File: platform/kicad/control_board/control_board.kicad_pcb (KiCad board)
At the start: 2 copper layers, 131.5 x 81.5 mm, 55 parts, among them J1 DHT22, J10 ADC1,7, J11 Qwiic JST, J13 PJ-002A, J14 ROUTER 24V, J15 24V/5V OUT, J16 Conn_01x05_Pin, J2 DS18B20, J4 24V IN, J5 USB4120-03-C_REVA, J8 UART, J9 ADC1,6, K1 LCA717, K2 LCA717, K3 LCA717, K4 LCA717, U1 ESP32-DevKitC, U2 ACS722xLCTR-20AU, U3 AP63205WU-7

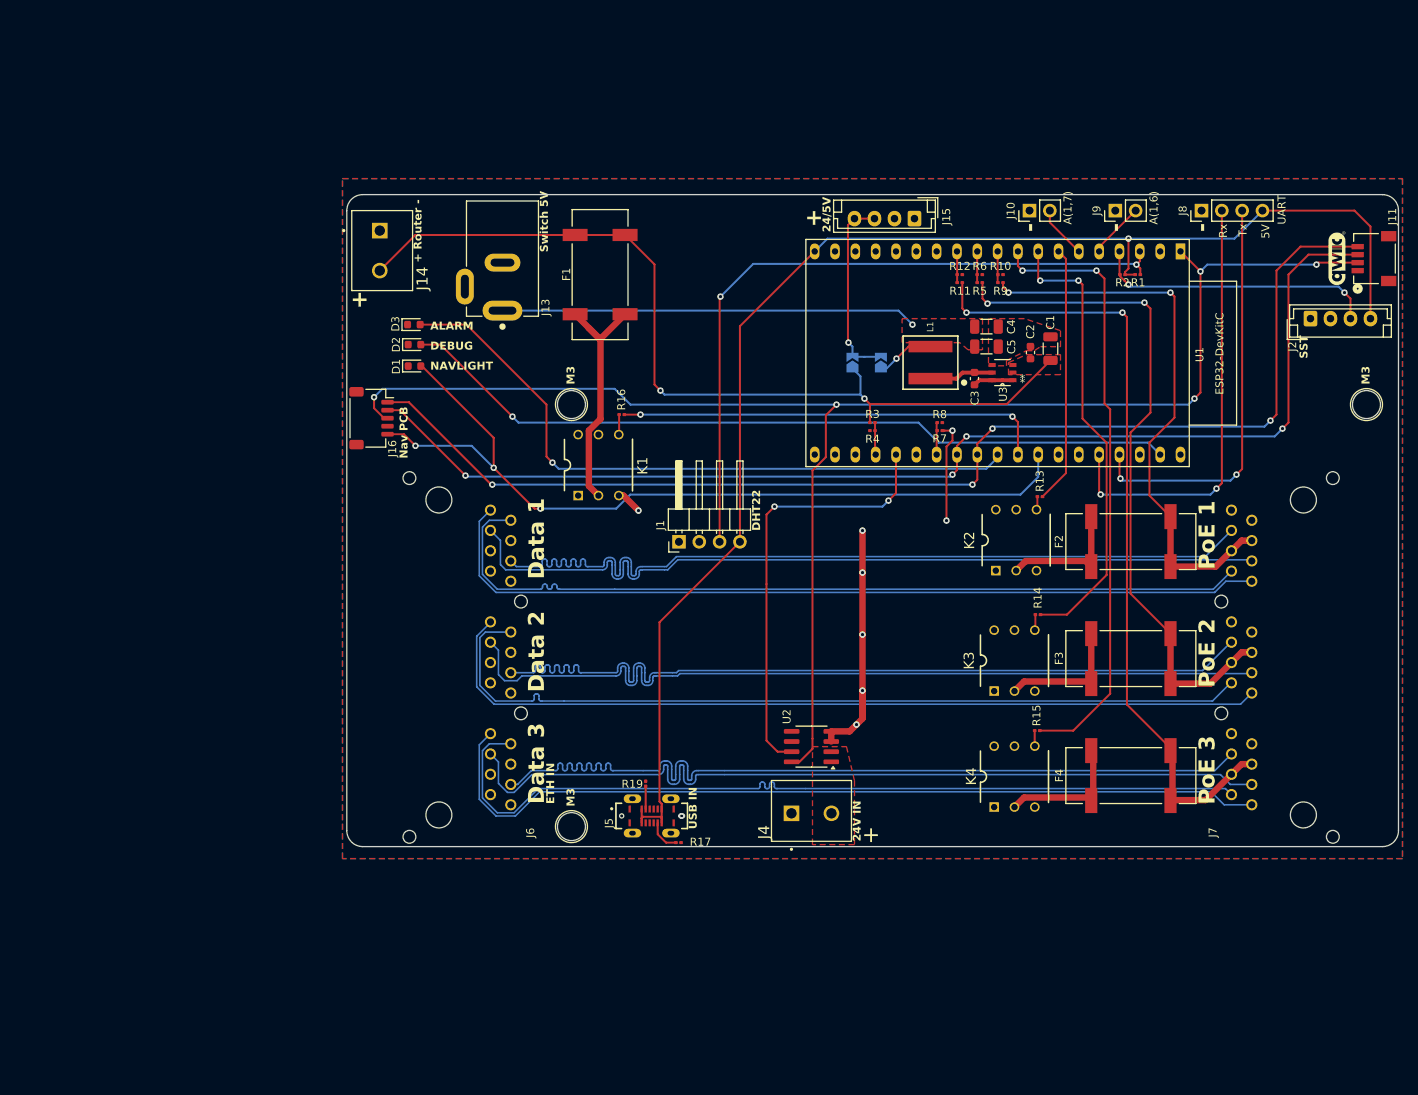
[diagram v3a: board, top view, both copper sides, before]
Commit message: Controller: Finalise Layout and Labelling (#3)
This change finalises the layout and tracks for the controller PCB, as well as the labelling.
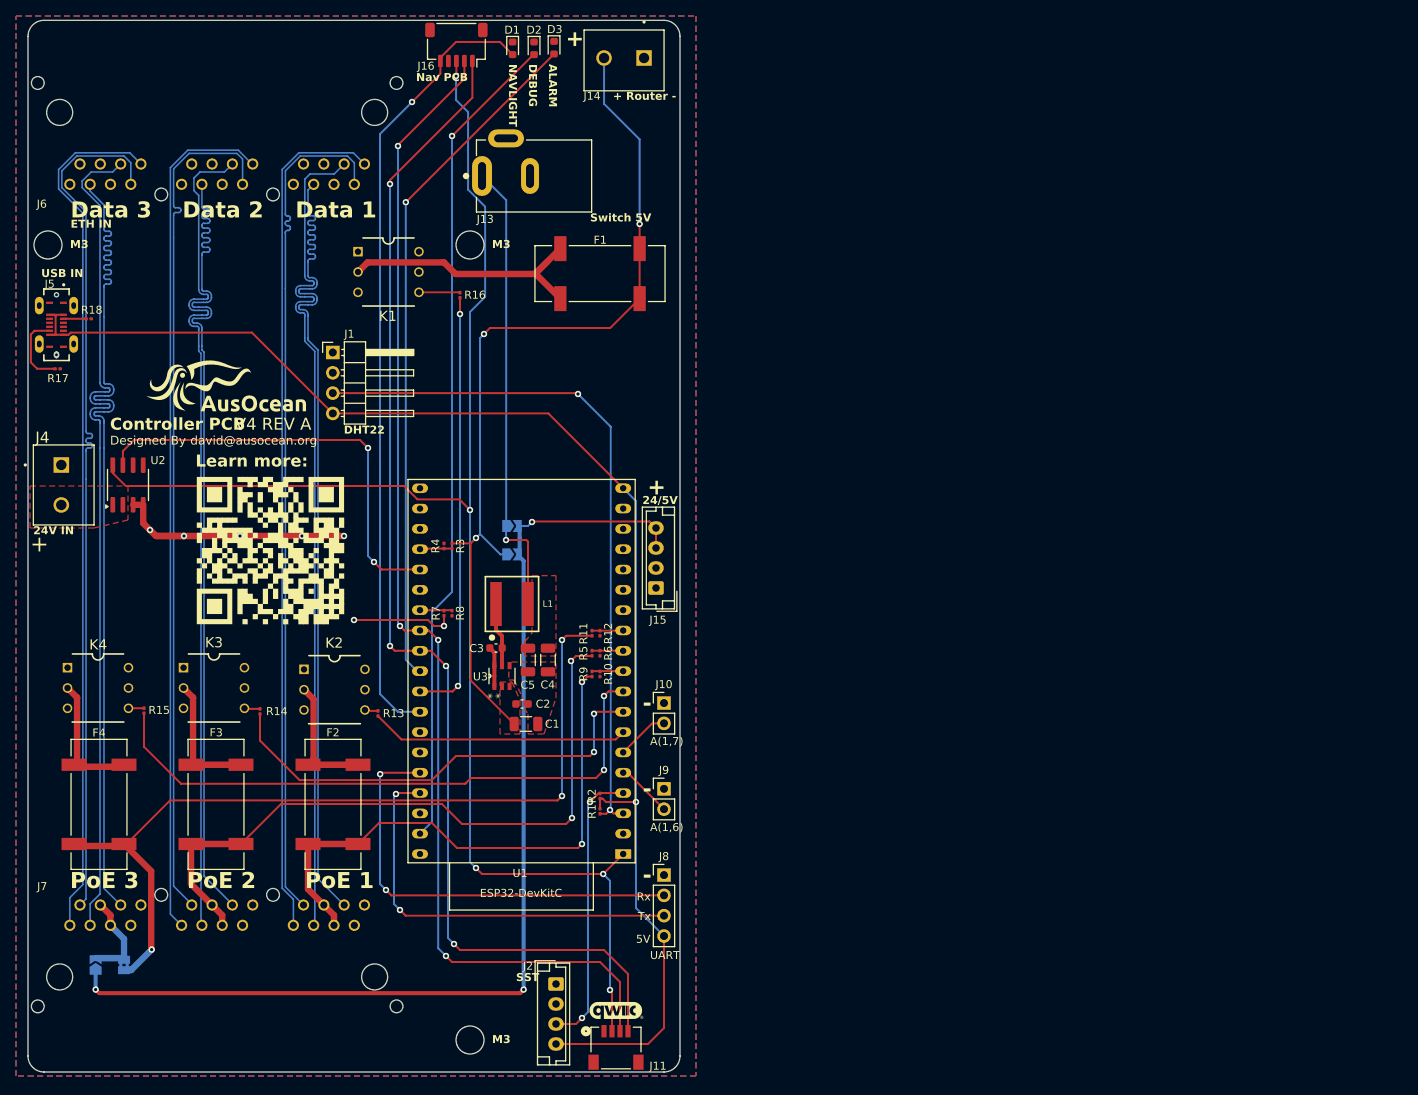
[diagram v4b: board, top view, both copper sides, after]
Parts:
- added G***: LOGO, LOGO, F.Cu at (110.4, 70.9)
- added JP3: SEL_P3, Jumper:SolderJumper-2_P1.3mm_Bridged2Bar_Pad1.0x1.5mm, B.Cu at (97.7, 143.3)
- added JP4: SEL_NW, Jumper:SolderJumper-2_P1.3mm_Open_TrianglePad1.0x1.5mm, B.Cu at (94.1, 143.3)
- moved J7 171.6 mm to (86.8, 155.7), turned to 0 degrees
- moved J11 136.8 mm to (159.2, 153.7), turned to 180 degrees
- moved G*** 130.1 mm to (159.2, 148.9), turned to 0 degrees
- moved F4 129.0 mm to (94.6, 123.2), turned to 180 degrees
- moved J2 125.7 mm to (151.7, 145.7), turned to -90 degrees
- moved F3 115.8 mm to (109.2, 123.2), turned to 180 degrees
- moved K4 115.1 mm to (94.4, 108.7), turned to 0 degrees
- moved R15 111.7 mm to (100.2, 111.5), turned to -90 degrees
- moved J8 106.8 mm to (165.2, 132.1), turned to 0 degrees
- moved F2 105.0 mm to (123.8, 123.2), turned to 180 degrees
- moved U1 102.6 mm to (160.1, 129.4), turned to 180 degrees
- moved J4 101.1 mm to (89.9, 80.8), turned to -90 degrees
- moved K3 100.1 mm to (108.9, 108.7), turned to 0 degrees
- moved R14 98.0 mm to (114.7, 111.6), turned to -90 degrees
- moved R17 97.6 mm to (89.4, 68.8)
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- renumbered R19 to R18
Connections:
- net 24VIN_IP renamed Net-(J4-Pin_2)
- J7 pad 4: P3_out -> P3_NW
- J7 pad 5: P3_out -> P3_NW
- JP1 pad 1: NW_5V -> NW_out
- JP2 pad 1: NW_out -> NW_5V
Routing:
- net 5-24VOUT: track 23.9 -> 134.6 mm, vias 1 -> 3
- net P3_NW: track 0.00 -> 11.7 mm
- net P3_out: track 98.8 -> 107.0 mm, vias 2 -> 3
- net Navlight: track 106.2 -> 99.1 mm, vias 3 -> 1
- net LED0: track 98.1 -> 103.3 mm
- net Net-(J5-CC2): track 4.18 -> 9.38 mm
- net +3V3: track 195.2 -> 190.8 mm
- net 24VIN: track 48.9 -> 45.6 mm, vias 8 -> 7
- net Net-(K1--_LOAD): track 31.5 -> 34.1 mm
- net Net-(K1-+_CONTROL): track 2.52 -> 5.15 mm
- net NW_5V: track 59.3 -> 57.4 mm, vias 2 -> 1
- net Alarm_LED: track 85.1 -> 86.5 mm
- net NW_out: track 111.5 -> 112.4 mm, vias 2 -> 3
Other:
- board size 131.5 x 81.5 mm -> 81.5 x 131.5 mm
- board text added: "1. Not using additional power - Do nothing 2. Using 24/5V JST (J12) - Select 24V or 5V using JP1 and JP2 3. Using PoE 3 for PoE network device - Select 24V or 5V using JP1 and JP2 - Cut JP3 and solder JP4"
- board text added: "24V"
- board text added: "Additional Network Power Setup:"
- board text added: "Controller PCB"
- board text added: "Designed By"
- board text added: "Learn more:"
- board text added: "NW"
- board text added: "P3"
- board text added: "Select only 5V (JP2) OR 24V (JP1)"
- board text added: "Select only P3-JP3 OR NW-JP4"
- board text added: "V4 REV A"
- board text added: "david@ausocean.org"

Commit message: Controller: Add External Watchdog (#3)
This change adds a STWD100YNYWY3F watchdog circuit which will be used to
trigger a reset if the ESP does not 'pat' it.
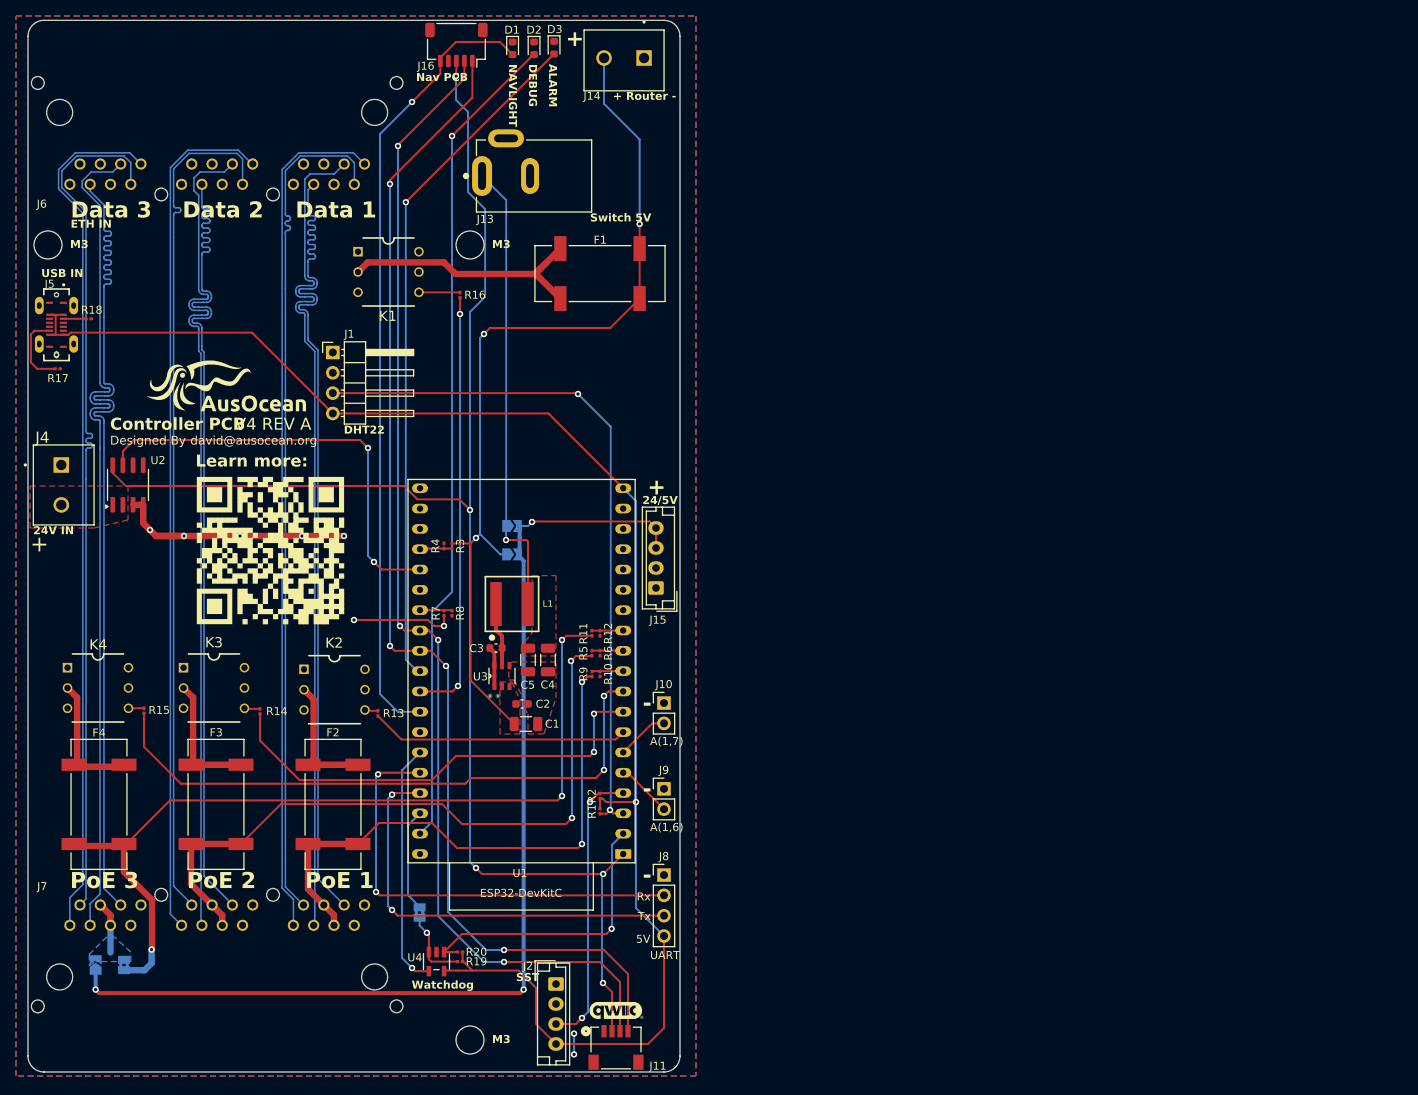
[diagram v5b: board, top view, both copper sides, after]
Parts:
- added JP5: USE_WD, Jumper:SolderJumper-2_P1.3mm_Bridged2Bar_Pad1.0x1.5mm, B.Cu at (134.6, 136.7)
- added R19: 4.7k, Resistor_SMD:R_0201_0603Metric, F.Cu at (139.7, 142.9)
- added R20: 10K, Resistor_SMD:R_0201_0603Metric, F.Cu at (139.7, 141.7)
- added U4: STWD100YNYWY3F, AusOcean:SOT23-5L_STM, F.Cu at (136.8, 142.9)
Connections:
- U1 pad 2: unconnected-(U1-CHIP_PU-Pad2) -> EN
- U1 pad 33: unconnected-(U1-GPIO21-Pad33) -> WD_IN
- U1 pad 36: unconnected-(U1-GPIO22-Pad36) -> WD_EN*
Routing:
- net EN: track 0.00 -> 36.3 mm, vias 0 -> 1
- net WD_IN: track 0.00 -> 30.7 mm, vias 0 -> 1
- net 5VIN: track 174.3 -> 197.4 mm
- net WD_EN*: track 0.00 -> 12.9 mm
- net Net-(JP5-A): track 0.00 -> 9.38 mm, vias 0 -> 1
- net P3_NW: track 11.7 -> 6.46 mm
- net GND: track 0.00 -> 2.60 mm, vias 0 -> 2
- net SDA: track 148.8 -> 146.5 mm
- net SCL: track 151.0 -> 149.1 mm
- net TX: track 51.3 -> 52.7 mm
- net RX: track 54.9 -> 56.3 mm
- added copper zone on B.Cu, net P3_NW
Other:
- board text added: "Disable External Watchdog"
- board text added: "Watchdog"

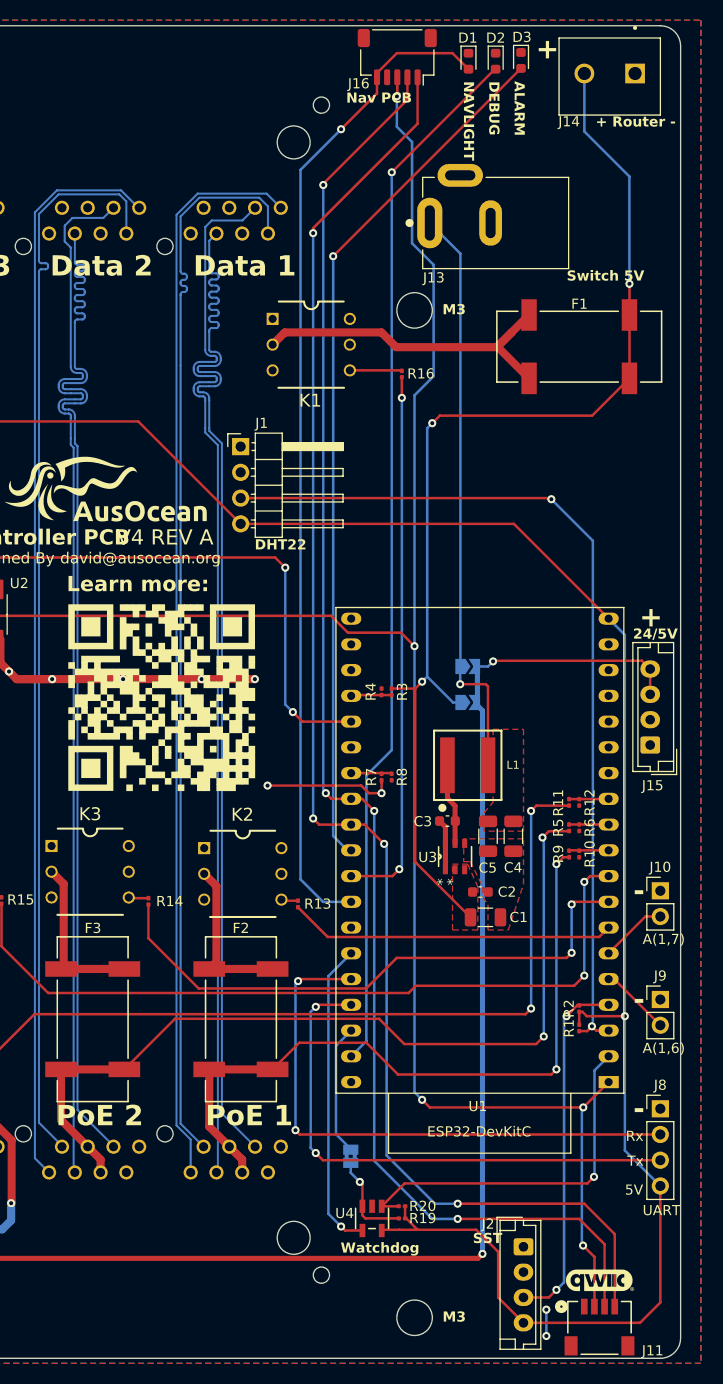
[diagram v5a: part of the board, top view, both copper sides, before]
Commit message: Control Board: Finalise V4 Rev A
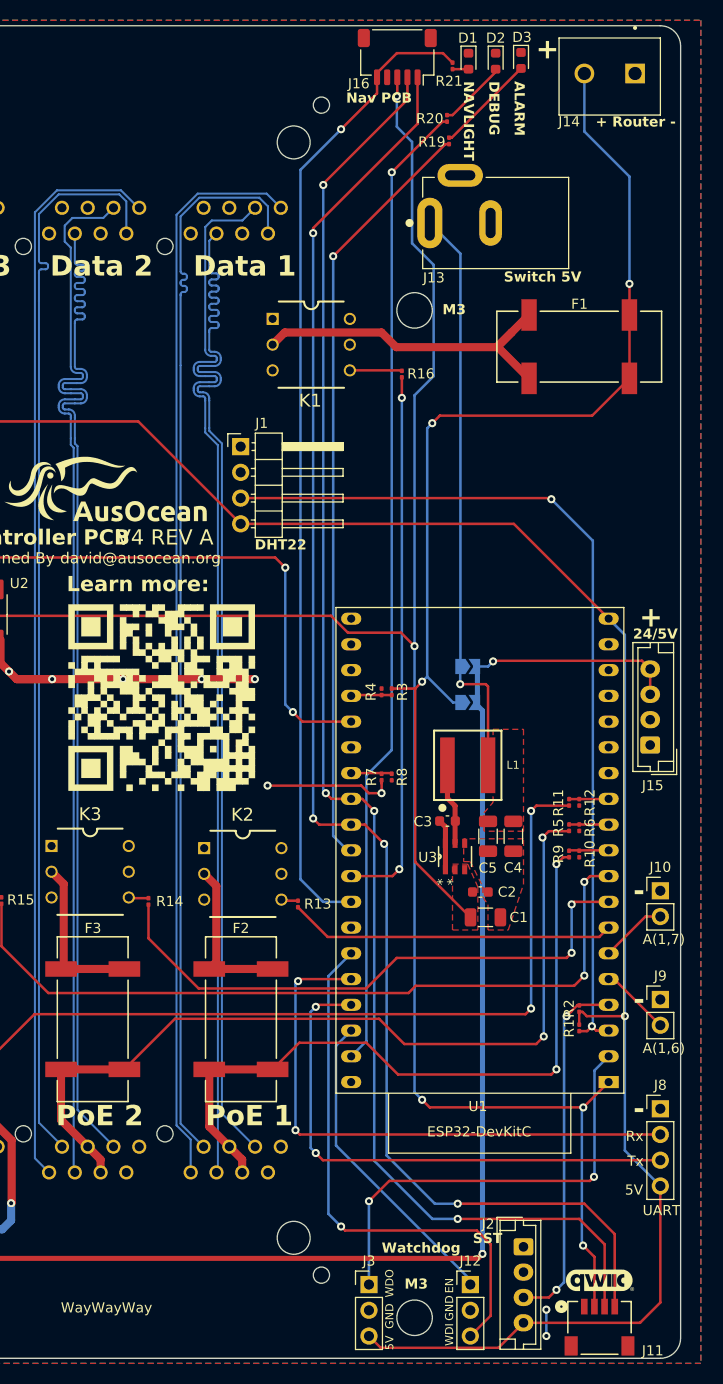
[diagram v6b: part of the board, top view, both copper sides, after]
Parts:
- removed JP5: USE_WD, Jumper:SolderJumper-2_P1.3mm_Bridged2Bar_Pad1.0x1.5mm
- removed U4: STWD100YNYWY3F, AusOcean:SOT23-5L_STM
- added J12: Conn_01x03, Connector_PinHeader_2.54mm:PinHeader_1x03_P2.54mm_Vertical, F.Cu at (146.4, 149.4)
- added J3: Conn_01x03, Connector_PinHeader_2.54mm:PinHeader_1x03_P2.54mm_Vertical, F.Cu at (136.4, 149.4)
- added R21: 280, Resistor_SMD:R_0201_0603Metric, F.Cu at (144.7, 29.2)
- D1: value LED -> LED (YELLOW)
- D2: value LED -> LED (BLUE)
- D3: value LED -> LED (RED)
- R19: value 4.7k -> 280
- R20: value 10K -> 120
- moved R20 107.4 mm to (144.1, 34.4), turned to 90 degrees
- moved R19 106.4 mm to (144.3, 36.6), turned to 90 degrees
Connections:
- D1 pad 2: Navlight -> Net-(D1-A)
- D2 pad 2: LED0 -> Net-(D2-A)
- D3 pad 2: Alarm_LED -> Net-(D3-A)
- R19 pad 1: 5VIN -> Alarm_LED
- R19 pad 2: Net-(JP5-A) -> Net-(D3-A)
- R20 pad 1: 5VIN -> LED0
- R20 pad 2: EN -> Net-(D2-A)
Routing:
- net WD_IN: track 30.7 -> 53.8 mm
- net WD_EN*: track 12.9 -> 31.2 mm
- net Alarm_LED: track 86.5 -> 76.3 mm
- net Net-(D3-A): track 0.00 -> 9.93 mm
- net Net-(JP5-A): track 9.38 -> 0.00 mm, vias 1 -> 0
- net EN: track 36.3 -> 43.9 mm, vias 1 -> 2
- net LED0: track 103.3 -> 96.4 mm
- net Net-(D2-A): track 0.00 -> 6.91 mm
- net 5VIN: track 197.4 -> 190.9 mm
- net Navlight: track 99.1 -> 97.2 mm
- net Net-(D1-A): track 0.00 -> 1.57 mm
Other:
- board text added: "EN"
- board text added: "GND"
- board text added: "WDI"
- board text added: "WDO"
- board text added: "WayWayWay"
